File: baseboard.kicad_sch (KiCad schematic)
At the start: 50 parts, among them J10 LCD_CHAR, J11 SERVO2, J12 BME280, J13 UART1, J14 FAN, J15 UART2, J16 AS7265X, J17 TFT_SPI, J5 POWER, J6 DCMI_CAMERA, J7 USER_GPIO, J8 SERVO1, J9 ADC_IN, Q1 BCP56, Q2 BCP56, Q3 BCP56, U1 LM2676S-5, U2 AMS1117-3.3

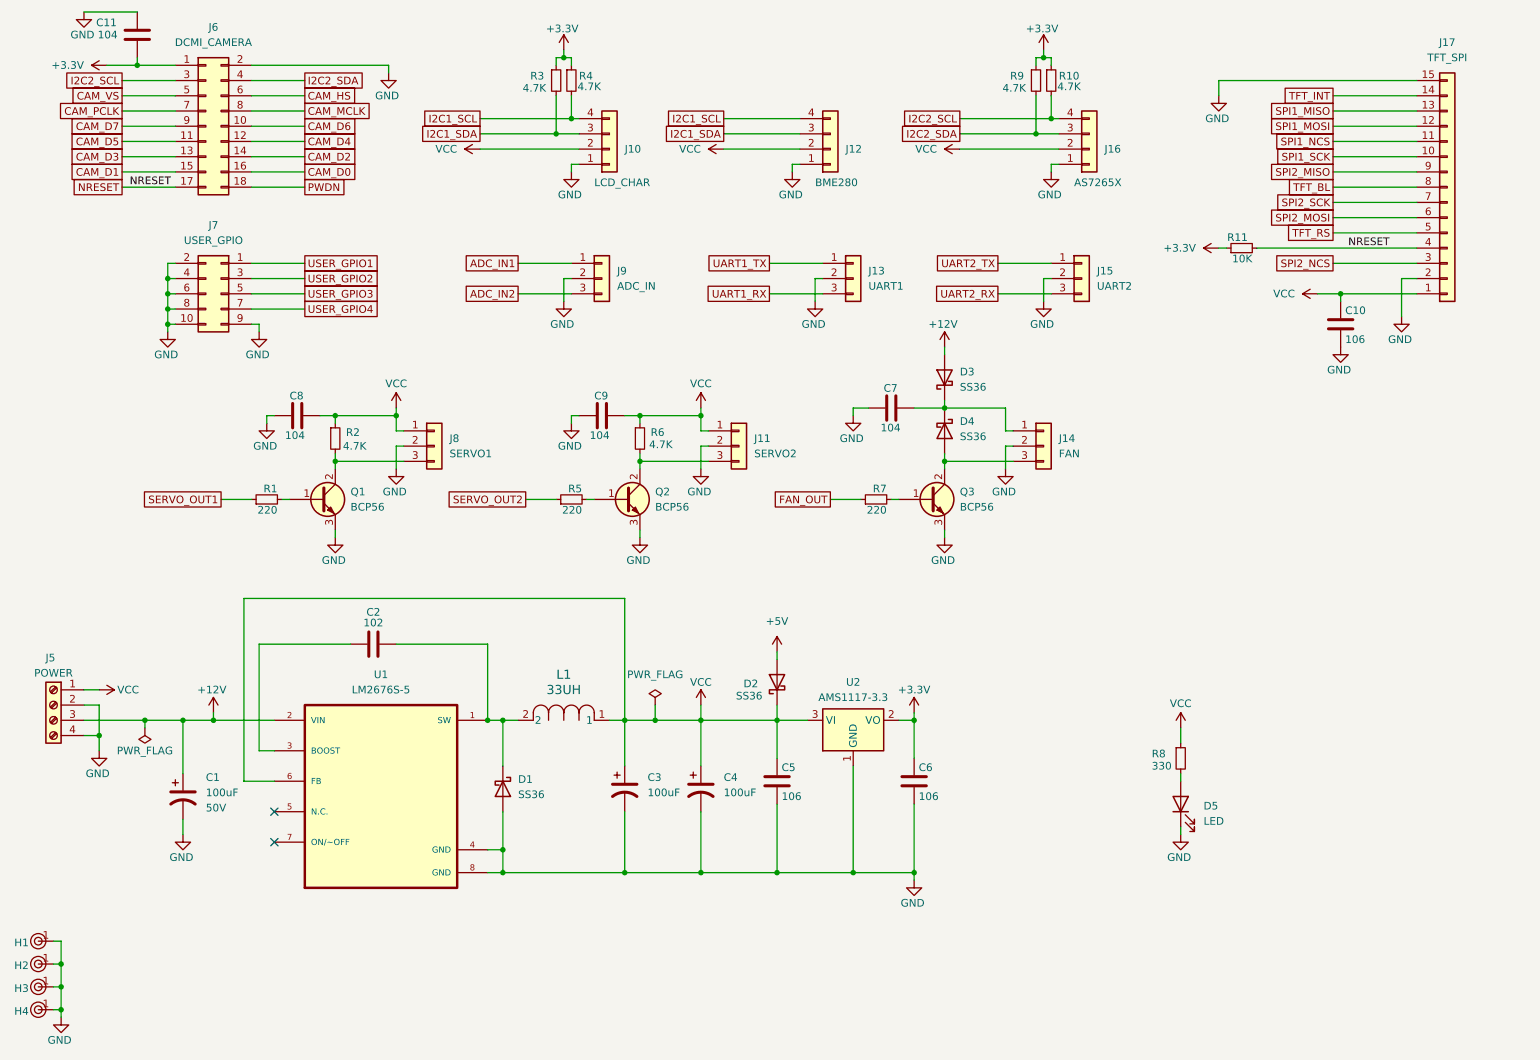
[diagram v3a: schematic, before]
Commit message: fix missing SPI2 on TFT_SPI
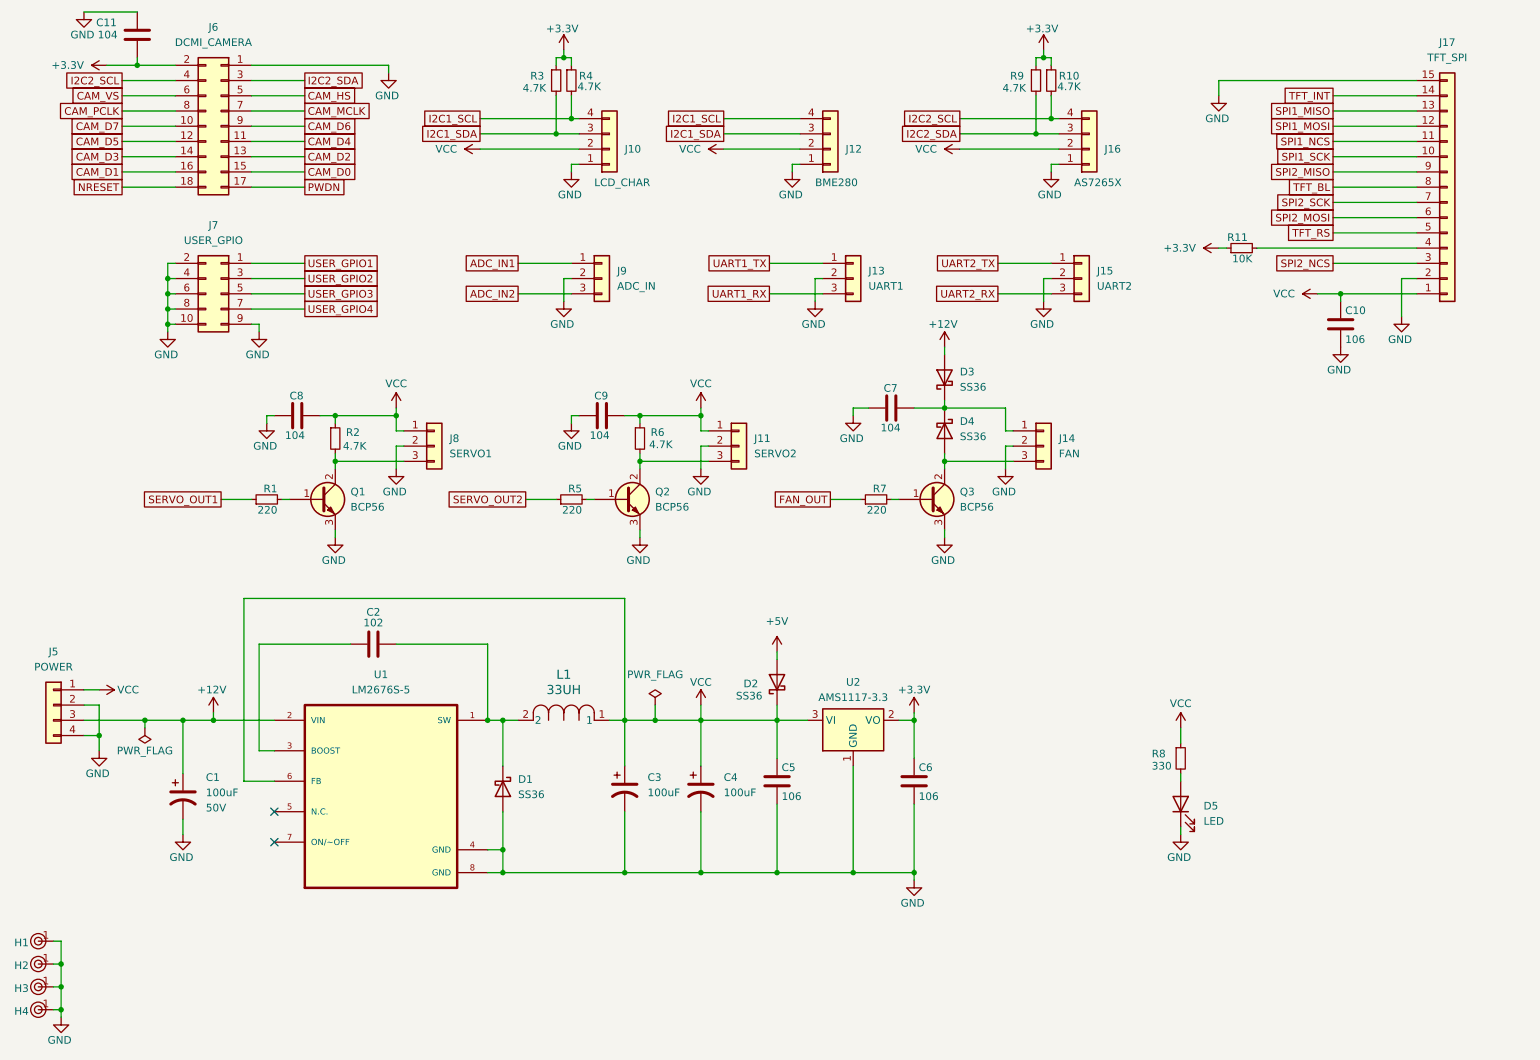
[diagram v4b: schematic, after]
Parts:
- removed J5: POWER, TerminalBlock:TerminalBlock_MaiXu_MX126-5.0-04P_1x04_P5.00mm, symbol Connector:Screw_Terminal_01x04
- added J5: POWER, Connector_PinHeader_2.54mm:PinHeader_1x04_P2.54mm_Vertical, symbol LM2676S-3.3_NOPB:Conn_01x04
- J6: footprint Connector_PinSocket_2.54mm:PinSocket_2x09_P2.54mm_Vertical -> Connector_PinHeader_2.54mm:PinHeader_2x09_P2.54mm_Vertical
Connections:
- net +12V: now also J5.3 (Pin_3)
- net +3.3V: now also J6.2 (Pin_2); no longer J6.1 (Pin_1)
- net CAM_D0: now also J6.15 (Pin_15); no longer J6.16 (Pin_16)
- net CAM_D1: now also J6.16 (Pin_16); no longer J6.15 (Pin_15)
- net CAM_D2: now also J6.13 (Pin_13); no longer J6.14 (Pin_14)
- net CAM_D3: now also J6.14 (Pin_14); no longer J6.13 (Pin_13)
- net CAM_D4: now also J6.11 (Pin_11); no longer J6.12 (Pin_12)
- net CAM_D5: now also J6.12 (Pin_12); no longer J6.11 (Pin_11)
- net CAM_D6: now also J6.9 (Pin_9); no longer J6.10 (Pin_10)
- net CAM_D7: now also J6.10 (Pin_10); no longer J6.9 (Pin_9)
- net CAM_HS: now also J6.5 (Pin_5); no longer J6.6 (Pin_6)
- net CAM_MCLK: now also J6.7 (Pin_7); no longer J6.8 (Pin_8)
- net CAM_PCLK: now also J6.8 (Pin_8); no longer J6.7 (Pin_7)
- net CAM_VS: now also J6.6 (Pin_6); no longer J6.5 (Pin_5)
- net GND: now also J6.1 (Pin_1), J5.2 (Pin_2), J5.4 (Pin_4); no longer J6.2 (Pin_2)
- net I2C2_SCL: now also J6.4 (Pin_4); no longer J6.3 (Pin_3)
- net I2C2_SDA: now also J6.3 (Pin_3); no longer J6.4 (Pin_4)
- net NRESET: now also J6.18 (Pin_18); no longer J17.4 (Pin_4), J6.17 (Pin_17), R11.2
- net PWDN: now also J6.17 (Pin_17); no longer J6.18 (Pin_18)
- net VCC: now also J5.1 (Pin_1)
- new net: J17.4 (Pin_4), R11.2
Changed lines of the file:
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@@
 	(wire
 		(pts
+			(xy 36.83 39.37) (xy 45.72 39.37)
+		)
+		(stroke
+			(width 0)
+			(type default)
+		)
+	)
+	(wire
+		(pts
 			(xy 226.06 57.15) (xy 252.73 57.15)
 		)
@@
 	(wire
 		(pts
-			(xy 45.72 36.83) (xy 36.83 36.83)
-		)
-		(stroke
-			(width 0)
-			(type default)
-		)
-	)
-	(wire
-		(pts
 			(xy 133.35 135.89) (xy 146.05 135.89)
 		)
@@
 	(wire
 		(pts
+			(xy 36.83 44.45) (xy 45.72 44.45)
+		)
+		(stroke
+			(width 0)
+			(type default)
+		)
+	)
+	(wire
+		(pts
 			(xy 123.19 92.71) (xy 123.19 93.98)
 		)
@@
 	(wire
 		(pts
+			(xy 36.83 31.75) (xy 45.72 31.75)
+		)
+		(stroke
+			(width 0)
+			(type default)
+		)
+	)
+	(wire
+		(pts
 			(xy 109.22 31.75) (xy 109.22 38.1)
 		)
@@
 	(wire
 		(pts
+			(xy 36.83 34.29) (xy 45.72 34.29)
+		)
+		(stroke
+			(width 0)
+			(type default)
+		)
+	)
+	(wire
+		(pts
 			(xy 184.15 90.17) (xy 184.15 93.98)
 		)
@@
 	(wire
 		(pts
-			(xy 45.72 46.99) (xy 36.83 46.99)
-		)
-		(stroke
-			(width 0)
-			(type default)
-		)
-	)
-	(wire
-		(pts
 			(xy 146.05 135.89) (xy 146.05 142.24)
 		)
@@
 	(wire
 		(pts
+			(xy 36.83 41.91) (xy 45.72 41.91)
+		)
+		(stroke
+			(width 0)
+			(type default)
+		)
+	)
+	(wire
+		(pts
 			(xy 58.42 29.21) (xy 67.31 29.21)
 		)
@@
 	(wire
 		(pts
-			(xy 45.72 31.75) (xy 36.83 31.75)
+			(xy 81.28 27.94) (xy 81.28 26.67)
 		)
 		(stroke
@@
 	(wire
 		(pts
-			(xy 81.28 27.94) (xy 81.28 26.67)
+			(xy 36.83 46.99) (xy 45.72 46.99)
 		)
 		(stroke
@@
 	(wire
 		(pts
-			(xy 184.15 83.82) (xy 184.15 87.63)
+			(xy 36.83 36.83) (xy 45.72 36.83)
 		)
 		(stroke
@@
 	(wire
 		(pts
-			(xy 158.75 83.82) (xy 158.75 85.09)
+			(xy 184.15 83.82) (xy 184.15 87.63)
 		)
 		(stroke
@@
 	(wire
 		(pts
-			(xy 110.49 25.4) (xy 109.22 25.4)
+			(xy 158.75 83.82) (xy 158.75 85.09)
 		)
 		(stroke
@@
 	(wire
 		(pts
-			(xy 81.28 26.67) (xy 58.42 26.67)
+			(xy 110.49 25.4) (xy 109.22 25.4)
 		)
 		(stroke
@@
 	(wire
 		(pts
-			(xy 113.03 85.09) (xy 111.76 85.09)
+			(xy 81.28 26.67) (xy 58.42 26.67)
 		)
 		(stroke
@@
 	(wire
 		(pts
-			(xy 30.48 17.78) (xy 39.37 17.78)
+			(xy 113.03 85.09) (xy 111.76 85.09)
 		)
 		(stroke
@@
 	(wire
 		(pts
-			(xy 165.1 99.06) (xy 166.37 99.06)
+			(xy 30.48 17.78) (xy 39.37 17.78)
 		)
 		(stroke
@@
 	(wire
 		(pts
-			(xy 213.36 137.16) (xy 213.36 139.7)
+			(xy 165.1 99.06) (xy 166.37 99.06)
 		)
 		(stroke
@@
 	(wire
 		(pts
-			(xy 45.72 39.37) (xy 36.83 39.37)
+			(xy 213.36 137.16) (xy 213.36 139.7)
 		)
 		(stroke
@@
 	(wire
 		(pts
-			(xy 45.72 44.45) (xy 36.83 44.45)
-		)
-		(stroke
-			(width 0)
-			(type default)
-		)
-	)
-	(wire
-		(pts
 			(xy 158.75 161.29) (xy 146.05 161.29)
 		)
@@
 	(wire
 		(pts
-			(xy 45.72 41.91) (xy 36.83 41.91)
-		)
-		(stroke
-			(width 0)
-			(type default)
-		)
-	)
-	(wire
-		(pts
 			(xy 123.19 91.44) (xy 123.19 92.71)
 		)
@@
 	(wire
 		(pts
-			(xy 45.72 34.29) (xy 36.83 34.29)
-		)
-		(stroke
-			(width 0)
-			(type default)
-		)
-	)
-	(wire
-		(pts
 			(xy 120.65 161.29) (xy 100.33 161.29)
 		)
@@
 		)
 	)
-	(label "NRESET"
-		(at 241.3 57.15 0)
-		(effects
-			(font
-				(size 1.27 1.27)
-			)
-			(justify left bottom)
-		)
-	)
-	(label "NRESET"
-		(at 38.1 46.99 0)
-		(effects
-			(font
-				(size 1.27 1.27)
-			)
-			(justify left bottom)
-		)
-	)
 	(global_label "SPI1_MISO"
 		(shape passive)
@@
 	)
 	(symbol
+		(lib_id "LM2676S-3.3_NOPB:Conn_01x04")
+		(at 25.4 133.35 0)
+		(mirror y)
+		(unit 1)
+		(exclude_from_sim no)
+		(in_bom yes)
+		(on_board yes)
+		(dnp no)
+		(fields_autoplaced yes)
+		(property "Reference" "J5"
+			(at 25.4 124.46 0)
+			(effects
+				(font
+					(size 1.27 1.27)
+				)
+			)
+		)
+		(property "Value" "POWER"
+			(at 25.4 127 0)
+			(effects
+				(font
+					(size 1.27 1.27)
+				)
+			)
+		)
+		(property "Footprint" "Connector_PinHeader_2.54mm:PinHeader_1x04_P2.54mm_Vertical"
+			(at 25.4 133.35 0)
+			(effects
+				(font
+					(size 1.27 1.27)
+				)
+				(hide yes)
+			)
+		)
+		(property "Datasheet" "~"
+			(at 25.4 133.35 0)
+			(effects
+				(font
+					(size 1.27 1.27)
+				)
+				(hide yes)
+			)
+		)
+		(property "Description" "Generic connector, single row, 01x04, script generated (kicad-library-utils/schlib/autogen/connector/)"
+			(at 25.4 133.35 0)
+			(effects
+				(font
+					(size 1.27 1.27)
+				)
+				(hide yes)
+			)
+		)
+		(pin "4"
+		)
+		(pin "3"
+		)
+		(pin "1"
+		)
+		(pin "2"
+		)
+		(instances
+			(project ""
+				(path "/1c72d2eb-7fb1-49fe-a026-e817f5a7ec43/16aff487-3924-4be3-b176-d1fab0e3868e"
+					(reference "J5")
+					(unit 1)
+				)
+			)
+		)
+	)
+	(symbol
 		(lib_id "PCM_JLCPCB-Manufacturing:Mounting Hole, 3mm, Via Stiched")
 		(at 22.86 176.53 0)
@@
 	)
 	(symbol
-		(lib_id "Connector:Screw_Terminal_01x04")
-		(at 25.4 133.35 0)
-		(mirror y)
-		(unit 1)
-		(exclude_from_sim no)
-		(in_bom yes)
-		(on_board yes)
-		(dnp no)
-		(property "Reference" "J5"
-			(at 24.892 125.476 0)
-			(effects
-				(font
-					(size 1.27 1.27)
-				)
-			)
-		)
-		(property "Value" "POWER"
-			(at 25.4 128.016 0)
-			(effects
-				(font
-					(size 1.27 1.27)
-				)
-			)
-		)
-		(property "Footprint" "TerminalBlock:TerminalBlock_MaiXu_MX126-5.0-04P_1x04_P5.00mm"
-			(at 25.4 133.35 0)
-			(effects
-				(font
-					(size 1.27 1.27)
-				)
-				(hide yes)
-			)
-		)
-		(property "Datasheet" "~"
-			(at 25.4 133.35 0)
-			(effects
-				(font
-					(size 1.27 1.27)
-				)
-				(hide yes)
-			)
-		)
-		(property "Description" "Generic screw terminal, single row, 01x04, script generated (kicad-library-utils/schlib/autogen/connector/)"
-			(at 25.4 133.35 0)
-			(effects
-				(font
-					(size 1.27 1.27)
-				)
-				(hide yes)
-			)
-		)
-		(pin "2"
-		)
-		(pin "1"
-		)
-		(pin "3"
-		)
-		(pin "4"
-		)
-		(instances
-			(project ""
-				(path "/1c72d2eb-7fb1-49fe-a026-e817f5a7ec43/16aff487-3924-4be3-b176-d1fab0e3868e"
-					(reference "J5")
-					(unit 1)
-				)
-			)
-		)
-	)
-	(symbol
 		(lib_id "LM2676S-3.3_NOPB:R_Small")
 		(at 109.22 29.21 0)
@@
 	(symbol
 		(lib_id "LM2676S-3.3_NOPB:Conn_02x09_Odd_Even")
-		(at 50.8 36.83 0)
+		(at 53.34 36.83 0)
+		(mirror y)
 		(unit 1)
 		(exclude_from_sim no)
@@
 		(on_board yes)
 		(dnp no)
-		(fields_autoplaced yes)
 		(property "Reference" "J6"
 			(at 52.07 20.32 0)
@@
 			)
 		)
-		(property "Footprint" "Connector_PinSocket_2.54mm:PinSocket_2x09_P2.54mm_Vertical"
-			(at 50.8 36.83 0)
+		(property "Footprint" "Connector_PinHeader_2.54mm:PinHeader_2x09_P2.54mm_Vertical"
+			(at 53.34 36.83 0)
 			(effects
 				(font
@@
 		)
 		(property "Datasheet" "~"
-			(at 50.8 36.83 0)
+			(at 53.34 36.83 0)
 			(effects
 				(font
@@
 		)
 		(property "Description" "Generic connector, double row, 02x09, odd/even pin numbering scheme (row 1 odd numbers, row 2 even numbers), script generated (kicad-library-utils/schlib/autogen/connector/)"
-			(at 50.8 36.83 0)
+			(at 53.34 36.83 0)
 			(effects
 				(font

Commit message: change capacitor footprint
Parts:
- C1: footprint Capacitor_THT:CP_Radial_D8.0mm_P5.00mm -> Capacitor_THT:CP_Radial_D8.0mm_P3.50mm
- C3, C4: value 100uF -> 220uF; footprint Capacitor_THT:CP_Radial_D8.0mm_P5.00mm -> Capacitor_THT:CP_Radial_D8.0mm_P3.50mm
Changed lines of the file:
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@@
 			)
 		)
-		(property "Footprint" "Capacitor_THT:CP_Radial_D8.0mm_P5.00mm"
+		(property "Footprint" "Capacitor_THT:CP_Radial_D8.0mm_P3.50mm"
 			(at 46.99 148.59 0)
 			(effects
@@
 			)
 		)
-		(property "Value" "100uF"
+		(property "Value" "220uF"
 			(at 137.16 147.9549 0)
 			(effects
@@
 			)
 		)
-		(property "Footprint" "Capacitor_THT:CP_Radial_D8.0mm_P5.00mm"
+		(property "Footprint" "Capacitor_THT:CP_Radial_D8.0mm_P3.50mm"
 			(at 133.35 147.32 0)
 			(effects
@@
 			)
 		)
-		(property "Value" "100uF"
+		(property "Value" "220uF"
 			(at 124.46 147.9549 0)
 			(effects
@@
 			)
 		)
-		(property "Footprint" "Capacitor_THT:CP_Radial_D8.0mm_P5.00mm"
+		(property "Footprint" "Capacitor_THT:CP_Radial_D8.0mm_P3.50mm"
 			(at 120.65 147.32 0)
 			(effects

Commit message: adjust schematic and PCB to reflect as build condition
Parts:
- removed D1: SS36, Diode_SMD:D_SMA, symbol LM2676S-3.3_NOPB:SS36
- added D1: SS56BF, Diode_SMD:D_SMB_Handsoldering, symbol PCM_Diode_Schottky_AKL:SS56BF
- C1: symbol LM2676S-3.3_NOPB:C_Polarized -> Library:C_Polarized
- C10, C11, C5, C6, C7, C8, C9: symbol LM2676S-3.3_NOPB:C -> Library:C
- C2: value 102 -> 103; footprint Capacitor_SMD:C_0603_1608Metric_Pad1.08x0.95mm_HandSolder -> Capacitor_SMD:C_0805_2012Metric_Pad1.18x1.45mm_HandSolder; symbol LM2676S-3.3_NOPB:C -> Library:C
- C3, C4: symbol LM2676S-3.3_NOPB:C_Polarized_US -> Library:C_Polarized_US
- D2, D3, D4: footprint Diode_SMD:D_SMA -> Diode_SMD:D_SMA_Handsoldering; symbol LM2676S-3.3_NOPB:SS36 -> Library:SS36
- D5: symbol LM2676S-3.3_NOPB:LED -> Library:LED
- H1, H2, H3, H4: symbol PCM_JLCPCB-Manufacturing:Mounting Hole, 3mm, Via Stiched -> Library:Mounting Hole, 3mm, Via Stiched
- J10, J12, J16, J5: symbol LM2676S-3.3_NOPB:Conn_01x04 -> Library:Conn_01x04
- J11, J13, J14, J15, J8, J9: symbol LM2676S-3.3_NOPB:Conn_01x03 -> Library:Conn_01x03
- J17: symbol Connector_Generic:Conn_01x15 -> Library:Conn_01x15
- J6: symbol LM2676S-3.3_NOPB:Conn_02x09_Odd_Even -> Library:Conn_02x09_Odd_Even
- J7: symbol Connector_Generic:Conn_02x05_Odd_Even -> Library:Conn_02x05_Odd_Even
- L1: symbol LM2676S-3.3_NOPB:CDRH104RNP-330NC -> Library:CDRH104RNP-330NC
- Q1, Q2, Q3: symbol PCM_Transistor_BJT_AKL:BCP56 -> Library:BCP56
- R1, R10, R2, R3, R4, R5, R6, R7, R9: symbol LM2676S-3.3_NOPB:R_Small -> Library:R_Small
- R11: value 10K -> 4.7K; symbol LM2676S-3.3_NOPB:R_Small -> Library:R_Small
- R8: value 330 -> 4.7K; symbol LM2676S-3.3_NOPB:R_Small -> Library:R_Small
- U1: symbol LM2676S-3.3_NOPB:LM2676S-3.3_NOPB -> Library:LM2676S-3.3_NOPB
- U2: symbol LM2676S-3.3_NOPB:AMS1117-3.3 -> Library:AMS1117-3.3
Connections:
- net GND: now also D1.2 (A)
- net at C2.2, L1.2, U1.1 (SW): now also D1.1 (K)

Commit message: archive symbols to local Library.kicad_sym
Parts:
- D1: symbol PCM_Diode_Schottky_AKL:SS56BF -> Library:SS56BF
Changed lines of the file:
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@@
 	)
 	(symbol
-		(lib_id "PCM_Diode_Schottky_AKL:SS56BF")
+		(lib_id "Library:SS56BF")
 		(at 100.33 147.32 90)
 		(unit 1)
